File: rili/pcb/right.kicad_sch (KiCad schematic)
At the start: 91 parts, among them J2 Conn_02x03_Odd_Even, J20 TPS43_FPC, J4 AudioJack4, SW100 SW_PUSH, SW101 SW_PUSH, SW102 SW_PUSH, SW103 SW_PUSH, SW104 SW_PUSH, SW105 SW_PUSH, SW74 SW_PUSH, SW75 SW_PUSH, SW76 SW_PUSH, SW77 SW_PUSH, SW82 SW_PUSH, SW83 SW_PUSH, SW84 SW_PUSH, SW85 SW_PUSH, SW88 SW_PUSH, SW89 SW_PUSH, SW90 SW_PUSH, SW91 SW_PUSH, SW92 SW_PUSH, SW93 SW_PUSH, SW94 SW_PUSH, SW95 SW_PUSH, SW96 SW_PUSH, SW97 SW_PUSH, SW98 SW_PUSH, SW99 SW_PUSH, U1 ESP32-S3-WROOM-1, U10 SiP32431DR3, U13 D, U14 D, U8 NRF24L01_Breakout, U9 SRV05-4

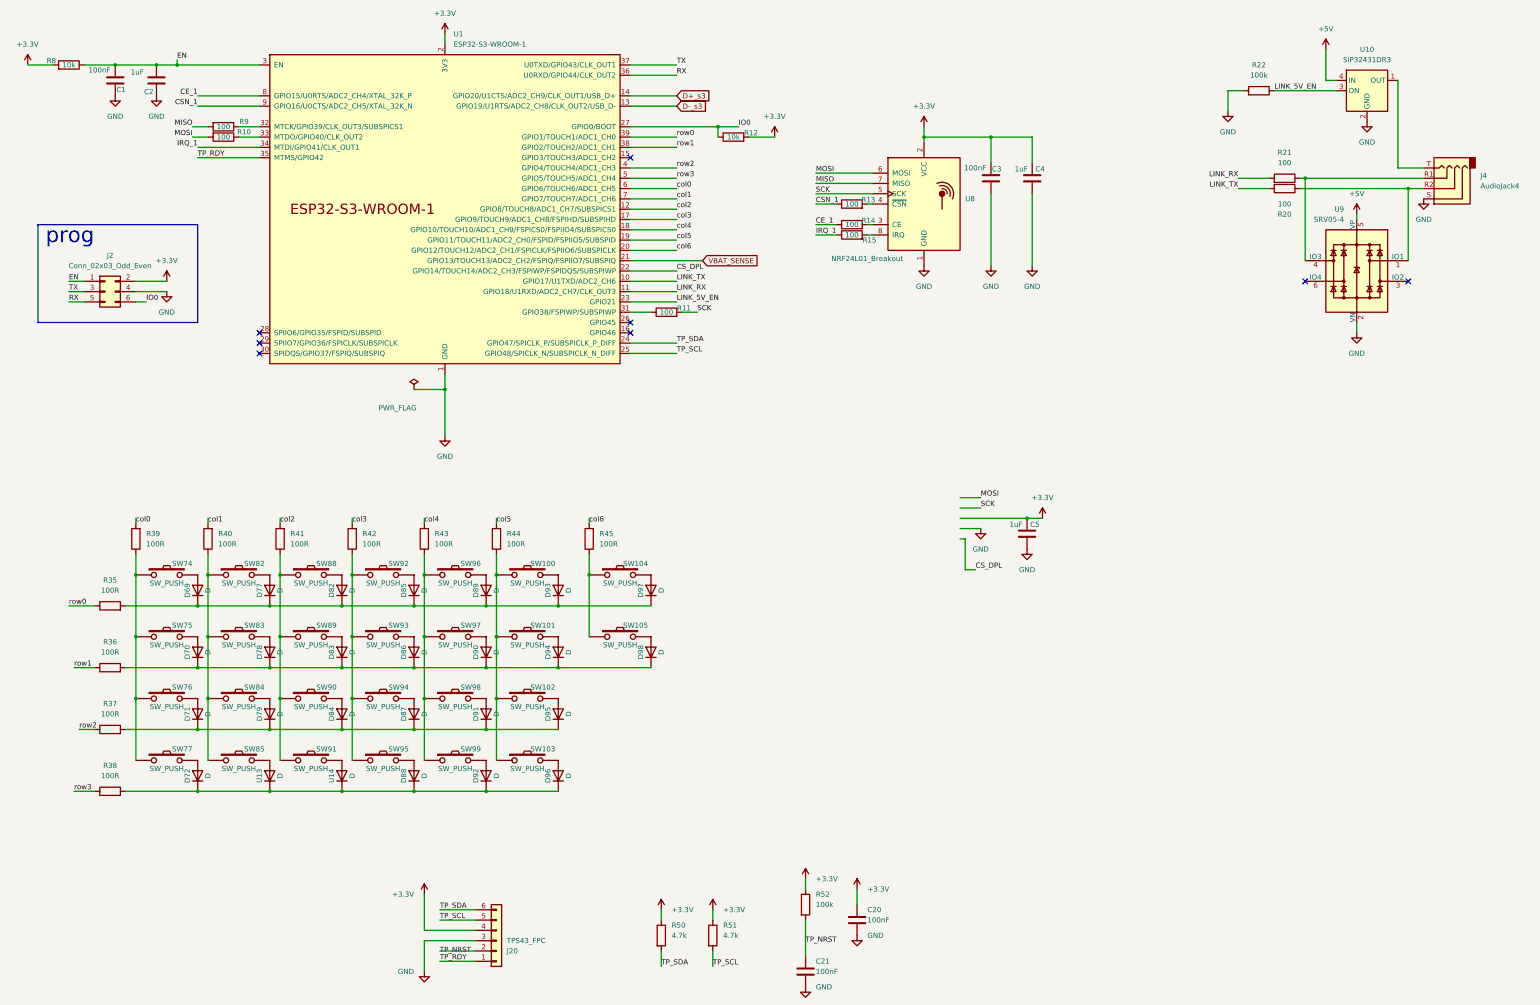
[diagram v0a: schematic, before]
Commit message: schéma v2 COMPLET : les deux moitiés — ERC 0 erreur
Architecture finale (brainstorm + nuit de réflexion, décision Mae) :
asymétrie d'origine confirmée — UN seul coffre.
- Gauche (s3/bat/usb/p4) : S3 + matrice + trackpad TPS43 + alim 16340
  + USB-C + hub CH334R + coffre P4 (SD multi-ISO, PGP, prog-via-hub)
- Droite (right/bat_right/usb_right, NOUVELLES feuilles) : S3 + matrice
  + écran Sharp + alim 16340 propre + USB-C simple (USBLC6 direct, sans hub)

Génération scriptée (make_droite/make_right_rails/cleanup, scratchpad) :
copies s3→right (refs +200) et bat→bat_right (refs +300, rails +BATT_D/
VSYS_D/+3.3V_D), usb→usb_right (refs +400, hub/P4/prog retirés, USBLC6
→ D±_s3_d, +5V_D), rails gauche/droite séparés (GND seul commun, physique
via TRRS), populate tranché (écran→droite, trackpad→gauche), feuille
Matrix retirée (matrice droite incluse dans right), droite.kicad_sch
remplacé par right.kicad_sch.

Validation : ERC projet 0 erreur ; nets droite bouclés de bout en bout
(+BATT_D→+3.3V_D→MCU, USB→USBLC6→MCU, jauge→GPIO13). Baseline warnings
re-référencée 125→164 (libs legacy doublées par la 2e moitié).

Prochaine phase : LAYOUT (réconciliation PCB↔schéma en une passe,
placement, routage, panneau sécable, DRC).

Co-Authored-By: Claude Fable 5 <noreply@anthropic.com>
Claude-Session: https://claude.ai/code/session_01GfX5RmekmQi78Dm37qsT4Z
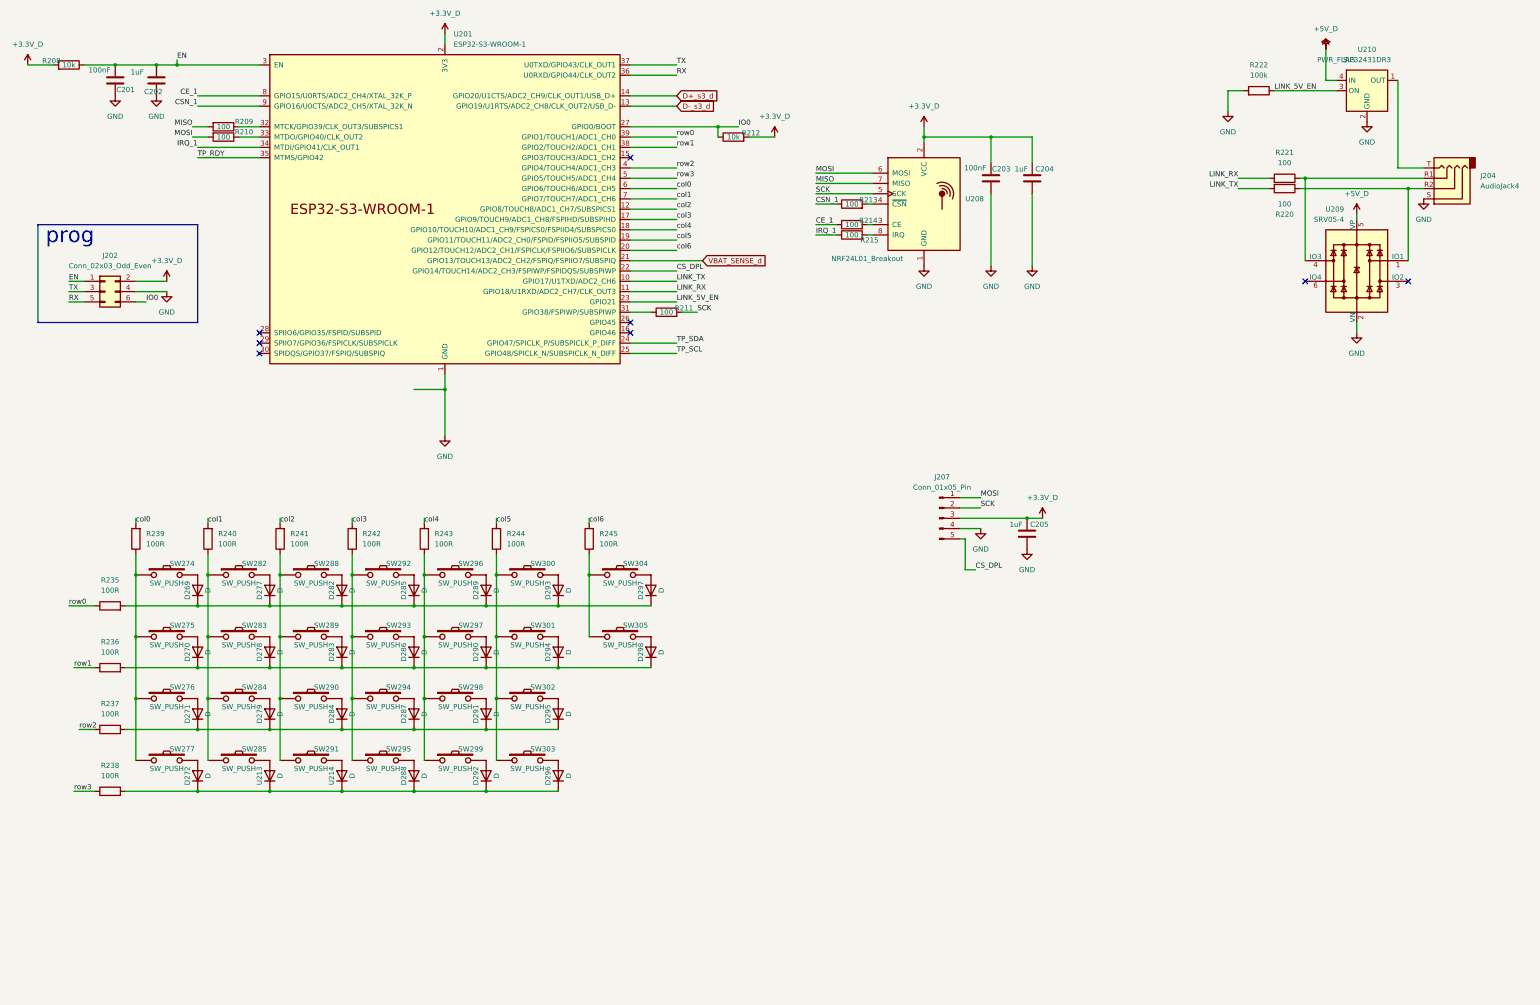
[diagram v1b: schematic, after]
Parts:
- removed C1, C3: 100nF, Capacitor_SMD:C_0603_1608Metric, symbol Device:C
- removed C2, C4, C5: 1uF, Capacitor_SMD:C_0603_1608Metric, symbol Device:C
- removed C20, C21: 100nF, Capacitor_SMD:C_0603_1608Metric_Pad1.08x0.95mm_HandSolder, symbol Device:C
- removed D69, D70, D71, D72, D77, D78, D79, D82, D83, D84, D85, D86, D87, D88, D89, D90, D91, D92, D93, D94, D95, D96, D97, D98, U13, U14: D, EKR82-footprint:Diode_TH_SOD123EKR, symbol Device:D
- removed J2: Conn_02x03_Odd_Even, Connector_PinHeader_1.27mm:PinHeader_2x03_P1.27mm_Vertical, symbol Connector_Generic:Conn_02x03_Odd_Even
- removed J20: TPS43_FPC, Connector_PinHeader_2.54mm:PinHeader_1x06_P2.54mm_Vertical, symbol Connector_Generic:Conn_01x06
- removed J4: AudioJack4, symbol Connector_Audio:AudioJack4
- removed R10, R11, R13, R14, R15, R9: 100, Resistor_SMD:R_0603_1608Metric, symbol Device:R
- removed R12, R8: 10k, Resistor_SMD:R_0603_1608Metric, symbol Device:R
- removed R20, R21: 100, Resistor_SMD:R_0603_1608Metric_Pad0.98x0.95mm_HandSolder, symbol Device:R
- removed R22, R52: 100k, Resistor_SMD:R_0603_1608Metric_Pad0.98x0.95mm_HandSolder, symbol Device:R
- removed R35, R36, R37, R38, R39, R40, R41, R42, R43, R44, R45: 100R, Resistor_SMD:R_0603_1608Metric_Pad0.98x0.95mm_HandSolder, symbol Device:R
- removed R50, R51: 4.7k, Resistor_SMD:R_0603_1608Metric_Pad0.98x0.95mm_HandSolder, symbol Device:R
- removed SW100, SW101, SW102, SW103, SW104, SW105, SW74, SW75, SW76, SW77, SW82, SW83, SW84, SW85, SW88, SW89, SW90, SW91, SW92, SW93, SW94, SW95, SW96, SW97, SW98, SW99: SW_PUSH, PMW3360:SW_Hotswap_Kailh_Choc_V1V2_1.00u, symbol corne-cherry-rescue:SW_PUSH-kbd-corne-cherry-rescue
- removed U1: ESP32-S3-WROOM-1, PCM_Espressif:ESP32-S3-WROOM-1U, symbol PCM_Espressif:ESP32-S3-WROOM-1
- removed U10: SiP32431DR3, Package_TO_SOT_SMD:SOT-363_SC-70-6, symbol Power_Management:SiP32431DR3
- removed U8: NRF24L01_Breakout, MaeLid:NRF24L01, symbol RF:NRF24L01_Breakout
- removed U9: SRV05-4, Package_TO_SOT_SMD:SOT-23-6, symbol Power_Protection:SRV05-4
- added C201, C203: 100nF, Capacitor_SMD:C_0603_1608Metric, symbol Device:C
- added C202, C204, C205: 1uF, Capacitor_SMD:C_0603_1608Metric, symbol Device:C
- added D269, D270, D271, D272, D277, D278, D279, D282, D283, D284, D285, D286, D287, D288, D289, D290, D291, D292, D293, D294, D295, D296, D297, D298, U213, U214: D, EKR82-footprint:Diode_TH_SOD123EKR, symbol Device:D
- added J202: Conn_02x03_Odd_Even, Connector_PinHeader_1.27mm:PinHeader_2x03_P1.27mm_Vertical, symbol Connector_Generic:Conn_02x03_Odd_Even
- added J204: AudioJack4, symbol Connector_Audio:AudioJack4
- added J207: Conn_01x05_Pin, Connector_PinHeader_2.54mm:PinHeader_1x05_P2.54mm_Vertical, symbol Connector:Conn_01x05_Pin
- added R208, R212: 10k, Resistor_SMD:R_0603_1608Metric, symbol Device:R
- added R209, R210, R211, R213, R214, R215: 100, Resistor_SMD:R_0603_1608Metric, symbol Device:R
- added R220, R221: 100, Resistor_SMD:R_0603_1608Metric_Pad0.98x0.95mm_HandSolder, symbol Device:R
- added R222: 100k, Resistor_SMD:R_0603_1608Metric_Pad0.98x0.95mm_HandSolder, symbol Device:R
- added R235, R236, R237, R238, R239, R240, R241, R242, R243, R244, R245: 100R, Resistor_SMD:R_0603_1608Metric_Pad0.98x0.95mm_HandSolder, symbol Device:R
- added SW274, SW275, SW276, SW277, SW282, SW283, SW284, SW285, SW288, SW289, SW290, SW291, SW292, SW293, SW294, SW295, SW296, SW297, SW298, SW299, SW300, SW301, SW302, SW303, SW304, SW305: SW_PUSH, PMW3360:SW_Hotswap_Kailh_Choc_V1V2_1.00u, symbol corne-cherry-rescue:SW_PUSH-kbd-corne-cherry-rescue
- added U201: ESP32-S3-WROOM-1, PCM_Espressif:ESP32-S3-WROOM-1U, symbol PCM_Espressif:ESP32-S3-WROOM-1
- added U208: NRF24L01_Breakout, MaeLid:NRF24L01, symbol RF:NRF24L01_Breakout
- added U209: SRV05-4, Package_TO_SOT_SMD:SOT-23-6, symbol Power_Protection:SRV05-4
- added U210: SiP32431DR3, Package_TO_SOT_SMD:SOT-363_SC-70-6, symbol Power_Management:SiP32431DR3
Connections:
- net CE_1: now also R214.1, U201.8 (GPIO15/U0RTS/ADC2_CH4/XTAL_32K_P)
- net CSN_1: now also R213.1, U201.9 (GPIO16/U0CTS/ADC2_CH5/XTAL_32K_N)
- net CS_DPL: now also J207.5 (Pin_5), U201.22 (GPIO14/TOUCH14/ADC2_CH3/FSPIWP/FSPIDQS/SUBSPIWP)
- net EN: now also C201.2, C202.2, J202.1 (Pin_1), R208.1, U201.3 (EN)
- net GND: now also C201.1, C202.1, C203.1, C204.1, C205.1, J202.4 (Pin_4), J204.S, J207.4 (Pin_4), R222.2, U201.1 (GND), U201.40 (GND), U201.41 (GND), U208.1 (GND), U209.2 (VN), U210.2 (GND), U210.5 (GND)
- net IO0: now also J202.6 (Pin_6), R212.1, U201.27 (GPIO0/BOOT)
- net IRQ_1: now also R215.1, U201.34 (MTDI/GPIO41/CLK_OUT1)
- net LINK_5V_EN: now also R222.1, U201.23 (GPIO21), U210.3 (ON)
- net LINK_RX: now also R221.2, U201.11 (GPIO18/U1RXD/ADC2_CH7/CLK_OUT3)
- net LINK_TX: now also R220.2, U201.10 (GPIO17/U1TXD/ADC2_CH6)
- net MISO: now also R209.2, U208.7 (MISO)
- net MOSI: now also J207.1 (Pin_1), R210.2, U208.6 (MOSI)
- net RX: now also J202.5 (Pin_5), U201.36 (U0RXD/GPIO44/CLK_OUT2)
- net SCK: now also J207.2 (Pin_2), R211.2, U208.5 (SCK)
- net TP_RDY: now also U201.35 (MTMS/GPIO42)
- net TP_SCL: now also U201.25 (GPIO48/SPICLK_N/SUBSPICLK_N_DIFF)
- net TP_SDA: now also U201.24 (GPIO47/SPICLK_P/SUBSPICLK_P_DIFF)
- net TX: now also J202.3 (Pin_3), U201.37 (U0TXD/GPIO43/CLK_OUT1)
- net col0: now also R239.2, U201.6 (GPIO6/TOUCH6/ADC1_CH5)
- net col1: now also R240.2, U201.7 (GPIO7/TOUCH7/ADC1_CH6)
- net col2: now also R241.2, U201.12 (GPIO8/TOUCH8/ADC1_CH7/SUBSPICS1)
- net col3: now also R242.2, U201.17 (GPIO9/TOUCH9/ADC1_CH8/FSPIHD/SUBSPIHD)
- net col4: now also R243.2, U201.18 (GPIO10/TOUCH10/ADC1_CH9/FSPICS0/FSPIIO4/SUBSPICS0)
- net col5: now also R244.2, U201.19 (GPIO11/TOUCH11/ADC2_CH0/FSPID/FSPIIO5/SUBSPID)
- net col6: now also R245.2, U201.20 (GPIO12/TOUCH12/ADC2_CH1/FSPICLK/FSPIIO6/SUBSPICLK)
- net row0: now also R235.1, U201.39 (GPIO1/TOUCH1/ADC1_CH0)
- net row1: now also R236.1, U201.38 (GPIO2/TOUCH2/ADC1_CH1)
- net row2: now also R237.1, U201.4 (GPIO4/TOUCH4/ADC1_CH3)
- net row3: now also R238.1, U201.5 (GPIO5/TOUCH5/ADC1_CH4)
- new net: D272.1 (K), D288.1 (K), D292.1 (K), D296.1 (K), R238.2, U213.1 (K), U214.1 (K)
- new net: D288.2 (A), SW295.2
- new net: D272.2 (A), SW277.2
- new net: D269.1 (K), D277.1 (K), D282.1 (K), D285.1 (K), D289.1 (K), D293.1 (K), D297.1 (K), R235.2
- new net: D282.2 (A), SW288.2
- new net: R240.1, SW282.1, SW283.1, SW284.1, SW285.1
- new net: D278.2 (A), SW283.2
- new net: R211.1, U201.31 (GPIO38/FSPIWP/SUBSPIWP)
- new net: R209.1, U201.32 (MTCK/GPIO39/CLK_OUT3/SUBSPICS1)
- new net: R210.1, U201.33 (MTDO/GPIO40/CLK_OUT2)
- new net: SW285.2, U213.2 (A)
- new net: J204.R1, R221.1, U209.4 (IO3)
- new net: D271.1 (K), D279.1 (K), D284.1 (K), D287.1 (K), D291.1 (K), D295.1 (K), R237.2
- new net: D271.2 (A), SW276.2
- new net: R241.1, SW288.1, SW289.1, SW290.1, SW291.1
- new net: R242.1, SW292.1, SW293.1, SW294.1, SW295.1
- new net: D285.2 (A), SW292.2
- new net: D270.1 (K), D278.1 (K), D283.1 (K), D286.1 (K), D290.1 (K), D294.1 (K), D298.1 (K), R236.2
- new net: D298.2 (A), SW305.2
- new net: R239.1, SW274.1, SW275.1, SW276.1, SW277.1
- new net: D269.2 (A), SW274.2
- new net: D289.2 (A), SW296.2
- new net: D287.2 (A), SW294.2
- new net: D290.2 (A), SW297.2
- new net: J204.R2, R220.1, U209.1 (IO1)
- new net: J204.T, U210.1 (OUT)
- new net: R214.2, U208.3 (CE)
- new net: D286.2 (A), SW293.2
- new net: R213.2, U208.4 (~{CSN})
- new net: R215.2, U208.8 (IRQ)
- new net: R244.1, SW300.1, SW301.1, SW302.1, SW303.1
- new net: D295.2 (A), SW302.2
- new net: D279.2 (A), SW284.2
- new net: D293.2 (A), SW300.2
- new net: D277.2 (A), SW282.2
- new net: D284.2 (A), SW290.2
- new net: D283.2 (A), SW289.2
- new net: D270.2 (A), SW275.2
- new net: SW291.2, U214.2 (A)
- new net: D292.2 (A), SW299.2
- new net: D294.2 (A), SW301.2
- new net: R243.1, SW296.1, SW297.1, SW298.1, SW299.1
- new net: D291.2 (A), SW298.2
- new net: D297.2 (A), SW304.2
- new net: R245.1, SW304.1, SW305.1
- new net: D296.2 (A), SW303.2
- new net +3.3V_D: C203.2, C204.2, C205.2, J202.2 (Pin_2), J207.3 (Pin_3), R208.2, R212.2, U201.2 (3V3), U208.2 (VCC)
- new net +5V_D: U209.5 (VP), U210.4 (IN)
- new net D+_s3_d: U201.14 (GPIO20/U1CTS/ADC2_CH9/CLK_OUT1/USB_D+)
- new net D-_s3_d: U201.13 (GPIO19/U1RTS/ADC2_CH8/CLK_OUT2/USB_D-)
- new net VBAT_SENSE_d: U201.21 (GPIO13/TOUCH13/ADC2_CH2/FSPIQ/FSPIIO7/SUBSPIQ)

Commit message: layout v2 : carte routée — PCB↔schéma réconciliés, BOM LCSC, TVS matrice, DRC 990→24
- réconciliation PCB↔schéma en une passe : 105 empreintes remariées (matrice ×2,
  module P4), 54 périmées supprimées, ~140 importées par F8 ; footprint TRRS
  MJ-4PP-9_rev3 créé (pads mappés de l'ancien design fonctionnel)
- placement : moitié droite générée au miroir exact du pré-placement gauche
  (axe x=188.46048), trous de montage symétrisés, origine de grille sur l'axe
- protection ESD matrice : 22 SD05C-01F (un par ligne, côté switchs des 100R,
  validés par partition de netlist) ; PWR_FLAG +5V_D réparé
- BOM LCSC dans les propriétés des symboles (32 composants : réfs, liens,
  notes d'achat) + annexe courses complète au plan v2 ; connecteur trackpad
  corrigé (ZIF Hirose FH12-6S-0.5SH, réf MNT Reform)
- règles JLCPCB (planchers DRC + classes Default/Power re-branchées v2),
  passage 4 couches, routage complet des deux moitiés
- gerbers v1 corne-cherry retirés (obsolètes)
- baselines tripwire re-référencées : DRC 990→24 erreurs / 208→17 warnings,
  ERC 0 erreur / 200 warnings (53 fantômes headless documentés)

Co-Authored-By: Claude Fable 5 <noreply@anthropic.com>
Claude-Session: https://claude.ai/code/session_01GfX5RmekmQi78Dm37qsT4Z
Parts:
- added D111, D112, D113, D114, D115, D116, D117, D118, D119, D120, D121: SD05C-01F, Diode_SMD:D_SOD-323, symbol Diode:SD05C-01F
- added H1, H2, H3, H4: MountingHole_Pad_MP, MountingHole:MountingHole_3.2mm_M3_DIN965_Pad, symbol Mechanical:MountingHole_Pad_MP
- D1: renamed from D269; footprint EKR82-footprint:Diode_TH_SOD123EKR -> Diode_SMD:D_SOD-123
- D10: renamed from D277; footprint EKR82-footprint:Diode_TH_SOD123EKR -> Diode_SMD:D_SOD-123
- D12: renamed from D278; footprint EKR82-footprint:Diode_TH_SOD123EKR -> Diode_SMD:D_SOD-123
- D14: renamed from D279; footprint EKR82-footprint:Diode_TH_SOD123EKR -> Diode_SMD:D_SOD-123
- D15: renamed from D282; footprint EKR82-footprint:Diode_TH_SOD123EKR -> Diode_SMD:D_SOD-123
- D17: renamed from D283; footprint EKR82-footprint:Diode_TH_SOD123EKR -> Diode_SMD:D_SOD-123
- D19: renamed from D284; footprint EKR82-footprint:Diode_TH_SOD123EKR -> Diode_SMD:D_SOD-123
- D22: renamed from D285; footprint EKR82-footprint:Diode_TH_SOD123EKR -> Diode_SMD:D_SOD-123
- D23: renamed from D286; footprint EKR82-footprint:Diode_TH_SOD123EKR -> Diode_SMD:D_SOD-123
- D25: renamed from D287; footprint EKR82-footprint:Diode_TH_SOD123EKR -> Diode_SMD:D_SOD-123
- D27: renamed from D288; footprint EKR82-footprint:Diode_TH_SOD123EKR -> Diode_SMD:D_SOD-123
- D29: renamed from D289; footprint EKR82-footprint:Diode_TH_SOD123EKR -> Diode_SMD:D_SOD-123
- D31: renamed from D290; footprint EKR82-footprint:Diode_TH_SOD123EKR -> Diode_SMD:D_SOD-123
- D34: renamed from D291; footprint EKR82-footprint:Diode_TH_SOD123EKR -> Diode_SMD:D_SOD-123
- D35: renamed from D292; footprint EKR82-footprint:Diode_TH_SOD123EKR -> Diode_SMD:D_SOD-123
- D37: renamed from D293; footprint EKR82-footprint:Diode_TH_SOD123EKR -> Diode_SMD:D_SOD-123
- D39: renamed from D294; footprint EKR82-footprint:Diode_TH_SOD123EKR -> Diode_SMD:D_SOD-123
- D4: renamed from D270; footprint EKR82-footprint:Diode_TH_SOD123EKR -> Diode_SMD:D_SOD-123
- D42: renamed from D295; footprint EKR82-footprint:Diode_TH_SOD123EKR -> Diode_SMD:D_SOD-123
- D44: renamed from D296; footprint EKR82-footprint:Diode_TH_SOD123EKR -> Diode_SMD:D_SOD-123
- D45: renamed from D297; footprint EKR82-footprint:Diode_TH_SOD123EKR -> Diode_SMD:D_SOD-123
- D47: renamed from D298; footprint EKR82-footprint:Diode_TH_SOD123EKR -> Diode_SMD:D_SOD-123
- D5: renamed from D271; footprint EKR82-footprint:Diode_TH_SOD123EKR -> Diode_SMD:D_SOD-123
- D7: renamed from D272; footprint EKR82-footprint:Diode_TH_SOD123EKR -> Diode_SMD:D_SOD-123
- J5: renamed from J204; footprint (none) -> EKR82-footprint:MJ-4PP-9_rev3; Achat (none) -> jack TRRS MJ-4PP-9 AliExpress; Lien (none) -> https://fr.aliexpress.com/item/33029465106.html
- SW11: renamed from SW283; footprint PMW3360:SW_Hotswap_Kailh_Choc_V1V2_1.00u -> key:SW_Cherry_MX_1.00u_PCB
- SW13: renamed from SW284; footprint PMW3360:SW_Hotswap_Kailh_Choc_V1V2_1.00u -> key:SW_Cherry_MX_1.00u_PCB
- SW16: renamed from SW285; footprint PMW3360:SW_Hotswap_Kailh_Choc_V1V2_1.00u -> key:SW_Cherry_MX_1.00u_PCB
- SW18: renamed from SW288; footprint PMW3360:SW_Hotswap_Kailh_Choc_V1V2_1.00u -> key:SW_Cherry_MX_1.00u_PCB
- SW2: renamed from SW274; footprint PMW3360:SW_Hotswap_Kailh_Choc_V1V2_1.00u -> key:SW_Cherry_MX_1.00u_PCB
- SW20: renamed from SW289; footprint PMW3360:SW_Hotswap_Kailh_Choc_V1V2_1.00u -> key:SW_Cherry_MX_1.00u_PCB
- SW22: renamed from SW290; footprint PMW3360:SW_Hotswap_Kailh_Choc_V1V2_1.00u -> key:SW_Cherry_MX_1.00u_PCB
- SW23: renamed from SW291; footprint PMW3360:SW_Hotswap_Kailh_Choc_V1V2_1.00u -> key:SW_Cherry_MX_1.00u_PCB
- SW25: renamed from SW292; footprint PMW3360:SW_Hotswap_Kailh_Choc_V1V2_1.00u -> key:SW_Cherry_MX_1.00u_PCB
- SW28: renamed from SW293; footprint PMW3360:SW_Hotswap_Kailh_Choc_V1V2_1.00u -> key:SW_Cherry_MX_1.00u_PCB
- SW29: renamed from SW294; footprint PMW3360:SW_Hotswap_Kailh_Choc_V1V2_1.00u -> key:SW_Cherry_MX_1.00u_PCB
- SW32: renamed from SW295; footprint PMW3360:SW_Hotswap_Kailh_Choc_V1V2_1.00u -> key:SW_Cherry_MX_1.00u_PCB
- SW34: renamed from SW296; footprint PMW3360:SW_Hotswap_Kailh_Choc_V1V2_1.00u -> key:SW_Cherry_MX_1.00u_PCB
- SW36: renamed from SW297; footprint PMW3360:SW_Hotswap_Kailh_Choc_V1V2_1.00u -> key:SW_Cherry_MX_1.00u_PCB
- SW37: renamed from SW298; footprint PMW3360:SW_Hotswap_Kailh_Choc_V1V2_1.00u -> key:SW_Cherry_MX_1.00u_PCB
- SW39: renamed from SW299; footprint PMW3360:SW_Hotswap_Kailh_Choc_V1V2_1.00u -> key:SW_Cherry_MX_1.00u_PCB
- SW4: renamed from SW275; footprint PMW3360:SW_Hotswap_Kailh_Choc_V1V2_1.00u -> key:SW_Cherry_MX_1.00u_PCB
- SW42: renamed from SW300; footprint PMW3360:SW_Hotswap_Kailh_Choc_V1V2_1.00u -> key:SW_Cherry_MX_1.00u_PCB
- SW44: renamed from SW301; footprint PMW3360:SW_Hotswap_Kailh_Choc_V1V2_1.00u -> key:SW_Cherry_MX_1.00u_PCB
- SW46: renamed from SW302; footprint PMW3360:SW_Hotswap_Kailh_Choc_V1V2_1.00u -> key:SW_Cherry_MX_1.00u_PCB
- SW48: renamed from SW303; footprint PMW3360:SW_Hotswap_Kailh_Choc_V1V2_1.00u -> key:SW_Cherry_MX_1.00u_PCB
- SW50: renamed from SW304; footprint PMW3360:SW_Hotswap_Kailh_Choc_V1V2_1.00u -> key:SW_Cherry_MX_1.00u_PCB
- SW51: renamed from SW305; footprint PMW3360:SW_Hotswap_Kailh_Choc_V1V2_1.00u -> key:SW_Cherry_MX_1.00u_PCB
- SW6: renamed from SW276; footprint PMW3360:SW_Hotswap_Kailh_Choc_V1V2_1.00u -> key:SW_Cherry_MX_1.00u_PCB
- SW7: renamed from SW277; footprint PMW3360:SW_Hotswap_Kailh_Choc_V1V2_1.00u -> key:SW_Cherry_MX_1.00u_PCB
- SW9: renamed from SW282; footprint PMW3360:SW_Hotswap_Kailh_Choc_V1V2_1.00u -> key:SW_Cherry_MX_1.00u_PCB
- U1: renamed from U213; footprint EKR82-footprint:Diode_TH_SOD123EKR -> Diode_SMD:D_SOD-123
- U10: renamed from U209; LCSC (none) -> C13612; Lien (none) -> https://lcsc.com/product-detail/C13612.html; Note achat (none) -> alt. budget Leiditech C384887
- U11: renamed from U210; LCSC (none) -> C141606; Lien (none) -> https://lcsc.com/product-detail/C141606.html
- U4: renamed from U214; footprint EKR82-footprint:Diode_TH_SOD123EKR -> Diode_SMD:D_SOD-123
- U5: renamed from U201; LCSC (none) -> C2913204; Lien (none) -> https://lcsc.com/product-detail/C2913204.html; Note achat (none) -> N8R2 ; si antenne externe (empreinte 1U) : C3013944
- U7: renamed from U208; Achat (none) -> module nRF24L01+ AliExpress (2x4 pin)
- renumbered C205 to C10, C204 to C12, C201 to C2, C202 to C4, C203 to C7, J202 to J2, J207 to J4, R208 to R1, R238 to R10, R239 to R12, R240 to R13, R209 to R15, R210 to R17, R241 to R19, R242 to R22, R243 to R24, R244 to R26, R245 to R28, R235 to R3, R211 to R31, R212 to R33, R213 to R37, R214 to R38, R215 to R40, R222 to R43, R221 to R44, R220 to R46, R236 to R5, R237 to R8
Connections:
- net GND: now also D111.2 (A2), D112.2 (A2), D113.2 (A2), D114.2 (A2), D115.2 (A2), D116.2 (A2), D117.2 (A2), D118.2 (A2), D119.2 (A2), D120.2 (A2), D121.2 (A2), H1.MP, H2.MP, H3.MP, H4.MP
- net col4: now also U5.19 (GPIO11/TOUCH11/ADC2_CH0/FSPID/FSPIIO5/SUBSPID); no longer U5.18 (GPIO10/TOUCH10/ADC1_CH9/FSPICS0/FSPIIO4/SUBSPICS0)
- net col5: now also U5.18 (GPIO10/TOUCH10/ADC1_CH9/FSPICS0/FSPIIO4/SUBSPICS0); no longer U5.19 (GPIO11/TOUCH11/ADC2_CH0/FSPID/FSPIIO5/SUBSPID)
- net col6: now also U5.39 (GPIO1/TOUCH1/ADC1_CH0); no longer U5.20 (GPIO12/TOUCH12/ADC2_CH1/FSPICLK/FSPIIO6/SUBSPICLK)
- net row0: now also U5.38 (GPIO2/TOUCH2/ADC1_CH1); no longer U5.39 (GPIO1/TOUCH1/ADC1_CH0)
- net row1: now also U5.20 (GPIO12/TOUCH12/ADC2_CH1/FSPICLK/FSPIIO6/SUBSPICLK); no longer U5.38 (GPIO2/TOUCH2/ADC1_CH1)
- net at D27.1 (K), D35.1 (K), D44.1 (K)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: now also D121.1 (A1)
- net at D1.1 (K), D10.1 (K), D15.1 (K)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: now also D118.1 (A1)
- net at R13.1, SW11.1, SW13.1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: now also D112.1 (A1)
- net at D14.1 (K), D19.1 (K), D25.1 (K)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: now also D120.1 (A1)
- net at R19.1, SW18.1, SW20.1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: now also D113.1 (A1)
- net at R22.1, SW25.1, SW28.1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: now also D114.1 (A1)
- net at D12.1 (K), D17.1 (K), D23.1 (K)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: now also D119.1 (A1)
- net at R12.1, SW2.1, SW4.1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: now also D111.1 (A1)
- net at R26.1, SW42.1, SW44.1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: now also D116.1 (A1)
- net at R24.1, SW34.1, SW36.1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: now also D115.1 (A1)
- net at R28.1, SW50.1, SW51.1: now also D117.1 (A1)
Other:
- moved on the sheet: R10, R12, R13, R19, R22, R24, R26, R28, R3, R5, R8

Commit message: layout : panneau vertical 2 rails dans le dépôt + baseline chantier
Panneau 185×212 (droite tournée 180°, rails + 8 tabs mouse-bites) appliqué par
Mae, F8 des passifs unifiés. Baseline DRC re-référencée 24/19 → 36/26 (état
panneau, finitions DRC prévues : pistes près des lignes de rupture, vias de
maillage orphelins dans les bandes sans cuivre).

Co-Authored-By: Claude Fable 5 <noreply@anthropic.com>
Claude-Session: https://claude.ai/code/session_01GfX5RmekmQi78Dm37qsT4Z
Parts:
- C10, C12, C4: footprint Capacitor_SMD:C_0603_1608Metric -> Capacitor_SMD:C_0805_2012Metric
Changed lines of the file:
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@@
 			)
 		)
-		(property "Footprint" "Capacitor_SMD:C_0603_1608Metric"
+		(property "Footprint" "Capacitor_SMD:C_0805_2012Metric"
 			(at 270.8148 57.15 0)
 			(hide yes)
@@
 			)
 		)
-		(property "Footprint" "Capacitor_SMD:C_0603_1608Metric"
+		(property "Footprint" "Capacitor_SMD:C_0805_2012Metric"
 			(at 269.5448 144.78 0)
 			(hide yes)
@@
 			)
 		)
-		(property "Footprint" "Capacitor_SMD:C_0603_1608Metric"
+		(property "Footprint" "Capacitor_SMD:C_0805_2012Metric"
 			(at 54.9148 33.02 0)
 			(hide yes)
